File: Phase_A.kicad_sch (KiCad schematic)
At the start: 12 parts

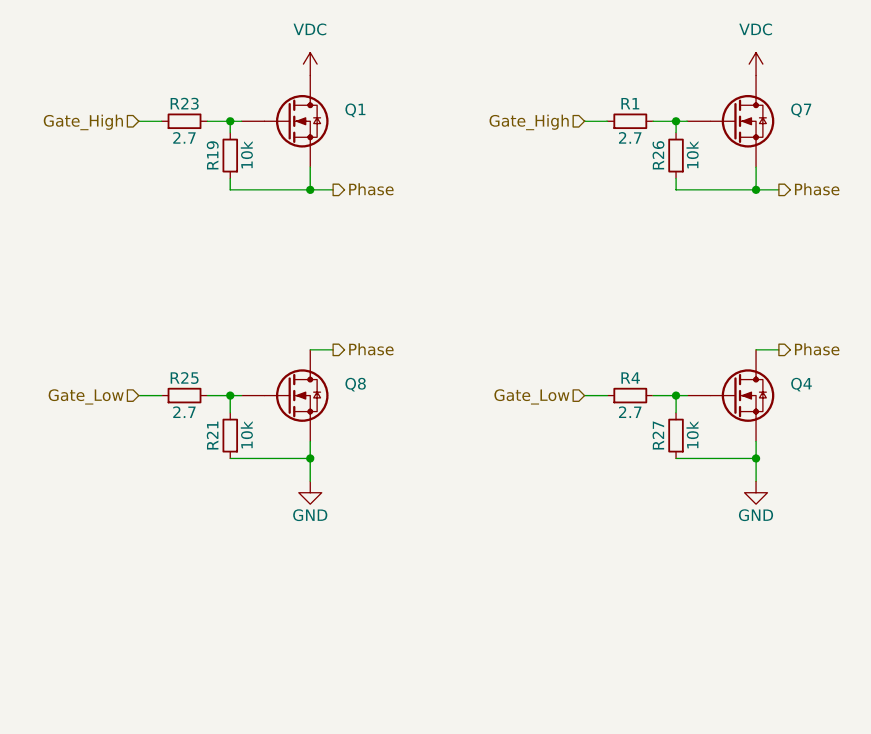
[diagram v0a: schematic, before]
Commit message: §3, §5, §6 схема: NetTie SW, ветвь выключения на позицию, C_gs, снабберы, RC на HI/LI
Driver.kicad_sch: SW драйвера — своя цепь через NetTie NT1–NT3; на HO и LO
R_on 0.82 Ом ∥ (D_off PMEG4010BEA + R_off 0 Ом), R106–R117, D30–D35; на HI/LI
R 0 Ом + C 100 пФ DNP (R118–R123, C118–C123).
Phase_A.kicad_sch: R_g 2.7 Ом 0805 -> 1 Ом 0603; C_gs 4.7 нФ DNP C100–C111;
снабберы LS и HS DNP (C112–C117, R100–R105).
ERC — 9 ошибок (база), netlist сверен по цепям: +57 компонентов, прочие связи
без изменений. ТЗ: Р3 — термистор остаётся на узле, Р10 — VDC→J6 можно
перекладывать.

Co-Authored-By: Claude Opus 5.5 <noreply@anthropic.com>
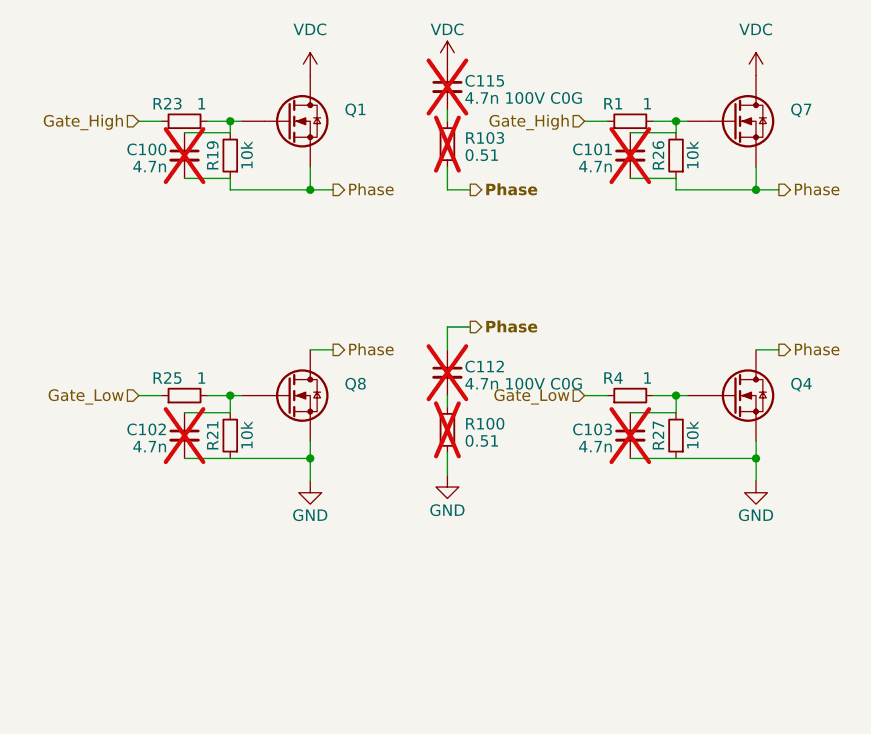
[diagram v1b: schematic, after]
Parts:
- added C100, C101, C102, C103: 4.7n, Capacitor_SMD:C_0603_1608Metric_Pad1.08x0.95mm_HandSolder, symbol Device:C_Small
- added C112, C115: 4.7n 100V C0G, Capacitor_SMD:C_0805_2012Metric_Pad1.18x1.45mm_HandSolder, symbol Device:C_Small
- added R100, R103: 0.51, Resistor_SMD:R_1206_3216Metric_Pad1.30x1.75mm_HandSolder, symbol Device:R_Small
- R1, R23, R25, R4: value 2.7 -> 1; footprint Resistor_SMD:R_0805_2012Metric_Pad1.20x1.40mm_HandSolder -> Resistor_SMD:R_0603_1608Metric_Pad0.98x0.95mm_HandSolder
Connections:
- net GND: now also C102.2, C103.2, R100.2
- net Phase: now also C100.2, C101.2, C112.1, R103.2
- net VDC: now also C115.1
- net at Q8.G, R21.2, R25.2: now also C102.1
- net at Q7.G, R1.2, R26.2: now also C101.1
- net at Q1.G, R19.2, R23.2: now also C100.1
- net at Q4.G, R27.2, R4.2: now also C103.1
- new net: C115.2, R103.1
- new net: C112.2, R100.1

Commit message: Схема, второй заход: ветвь выключения без R_off, керамика §4 (Р14, Р15)
R_off (R109–R111, R115–R117) убраны — D_off прямо от X к выводу драйвера;
R_on — 0603, D_off — стандартный SOD-323. Керамика петли C124–C135,
1 мкФ 100 В 1206, по 4 на фазу. ERC — 9 ошибок (база), netlist сверен.

Co-Authored-By: Claude Opus 5.5 <noreply@anthropic.com>
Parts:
- added C124, C125, C126, C127: 1u 100V X7R, Capacitor_SMD:C_1206_3216Metric_Pad1.33x1.80mm_HandSolder, symbol Device:C_Small
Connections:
- net GND: now also C124.2, C125.2, C126.2, C127.2
- net VDC: now also C124.1, C125.1, C126.1, C127.1

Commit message: WIP разводка: керамика §4 — по одному 1206 на фазу; лишние три на фазу убраны из схемы
1206 1u 100V (C124/C128/C132) в среднем ряду колонки стока HS, одинаково на
трёх фазах, у каждого своя пара виа (VDC и GND). Верхняя полоса над стоком
занята корпусами банок ЗПТ Ø10 (по футпринту до y 74.1), нижний ряд — R_g
нижнего HS; поэтому C125–C127, C129–C131, C133–C135 удалены из схемы и платы
(Р6, «по месту»). C110 переставлен вглубь полосы A (4 виа сдвинуты в полосе).
DRC: 0 ошибок, расхождений со схемой нет; ERC: 9 (база).

Co-Authored-By: Claude Opus 5.5 <noreply@anthropic.com>
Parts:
- removed C125, C126, C127: 1u 100V X7R, Capacitor_SMD:C_1206_3216Metric_Pad1.33x1.80mm_HandSolder, symbol Device:C_Small

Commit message: Д1, Д2: C_gs C100–C111 — 10 нФ C0G, ставятся; D_off D30–D35 — DNP (схема и плата); Д3 снят решением владельца
Co-Authored-By: Claude Opus 5.5 <noreply@anthropic.com>
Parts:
- C100, C101, C102, C103: value 4.7n -> 10n 50V C0G; Description P/N Capacitor SMD 50V -> Capacitor SMD 50V C0G; now fitted
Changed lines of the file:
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@@
 		(on_board yes)
 		(in_pos_files yes)
-		(dnp yes)
+		(dnp no)
 		(property "Reference" "C100"
 			(at 104.775 81.915 0)
@@
 			)
 		)
-		(property "Value" "4.7n"
+		(property "Value" "10n 50V C0G"
 			(at 104.775 83.82 0)
 			(show_name no)
@@
 			)
 		)
-		(property "Description P/N" "Capacitor SMD 50V"
+		(property "Description P/N" "Capacitor SMD 50V C0G"
 			(at 106.68 82.55 0)
 			(hide yes)
@@
 		(on_board yes)
 		(in_pos_files yes)
-		(dnp yes)
+		(dnp no)
 		(property "Reference" "C101"
 			(at 154.305 81.915 0)
@@
 			)
 		)
-		(property "Value" "4.7n"
+		(property "Value" "10n 50V C0G"
 			(at 154.305 83.82 0)
 			(show_name no)
@@
 			)
 		)
-		(property "Description P/N" "Capacitor SMD 50V"
+		(property "Description P/N" "Capacitor SMD 50V C0G"
 			(at 156.21 82.55 0)
 			(hide yes)
@@
 		(on_board yes)
 		(in_pos_files yes)
-		(dnp yes)
+		(dnp no)
 		(property "Reference" "C102"
 			(at 104.775 113.03 0)
@@
 			)
 		)
-		(property "Value" "4.7n"
+		(property "Value" "10n 50V C0G"
 			(at 104.775 114.935 0)
 			(show_name no)
@@
 			)
 		)
-		(property "Description P/N" "Capacitor SMD 50V"
+		(property "Description P/N" "Capacitor SMD 50V C0G"
 			(at 106.68 113.665 0)
 			(hide yes)
@@
 		(on_board yes)
 		(in_pos_files yes)
-		(dnp yes)
+		(dnp no)
 		(property "Reference" "C103"
 			(at 154.305 113.03 0)
@@
 			)
 		)
-		(property "Value" "4.7n"
+		(property "Value" "10n 50V C0G"
 			(at 154.305 114.935 0)
 			(show_name no)
@@
 			)
 		)
-		(property "Description P/N" "Capacitor SMD 50V"
+		(property "Description P/N" "Capacitor SMD 50V C0G"
 			(at 156.21 113.665 0)
 			(hide yes)

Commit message: Плата длиннее на 4 мм: банки ЗПТ, J4/J5, H1/H2 выше; снабберы §5 у выводов (C 0805 + R 0612 0.47 Ом, средняя точка — перемычка), 1206 C125/C129/C133 у стока HS, 0603 по две на фазу; DRC 0/0/0
Co-Authored-By: Claude Opus 5.5 <noreply@anthropic.com>
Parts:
- added C125: 1u 100V X7R, Capacitor_SMD:C_1206_3216Metric_Pad1.33x1.80mm_HandSolder, symbol Device:C_Small
- R100, R103: value 0.51 -> 0.47; footprint Resistor_SMD:R_1206_3216Metric_Pad1.30x1.75mm_HandSolder -> Resistor_SMD:R_0612_1632Metric_Pad1.18x3.40mm_HandSolder; Description P/N Resistor SMD 0.5W -> Resistor SMD 0612 1.5W
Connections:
- net GND: now also C125.2
- net VDC: now also C125.1
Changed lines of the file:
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@@
+	(symbol
+		(lib_id "Device:C_Small")
+		(at 120.65 137.16 0)
+		(unit 1)
+		(body_style 1)
+		(exclude_from_sim no)
+		(in_bom yes)
+		(on_board yes)
+		(in_pos_files yes)
+		(dnp no)
+		(property "Reference" "C125"
+			(at 121.92 136.525 0)
+			(show_name no)
+			(do_not_autoplace no)
+			(effects
+				(font
+					(size 1.27 1.27)
+				)
+				(justify left)
+			)
+		)
+		(property "Value" "1u 100V X7R"
+			(at 121.92 138.43 0)
+			(show_name no)
+			(do_not_autoplace no)
+			(effects
+				(font
+					(size 1.27 1.27)
+				)
+				(justify left)
+			)
+		)
+		(property "Footprint" "Capacitor_SMD:C_1206_3216Metric_Pad1.33x1.80mm_HandSolder"
+			(at 120.65 137.16 0)
+			(hide yes)
+			(show_name no)
+			(do_not_autoplace no)
+			(effects
+				(font
+					(size 1.27 1.27)
+				)
+			)
+		)
+		(property "Datasheet" ""
+			(at 120.65 137.16 0)
+			(hide yes)
+			(show_name no)
+			(do_not_autoplace no)
+			(effects
+				(font
+					(size 1.27 1.27)
+				)
+			)
+		)
+		(property "Description" ""
+			(at 120.65 137.16 0)
+			(hide yes)
+			(show_name no)
+			(do_not_autoplace no)
+			(effects
+				(font
+					(size 1.27 1.27)
+				)
+			)
+		)
+		(property "Description P/N" "Capacitor SMD 100V X7R"
+			(at 120.65 137.16 0)
+			(hide yes)
+			(show_name no)
+			(do_not_autoplace no)
+			(effects
+				(font
+					(size 1.27 1.27)
+				)
+			)
+		)
+		(pin "1"
+		)
+		(pin "2"
+		)
+		(instances
+			(project "Power"
+				(path "/7ff38f8b-11c9-43a1-8b76-b5e8c8de18e0/f977a2eb-d10b-44d6-a07c-b8311dd9b73f"
+					(reference "C125")
+					(unit 1)
+				)
+				(path "/7ff38f8b-11c9-43a1-8b76-b5e8c8de18e0/7176583c-694b-43e7-a08f-7dfec6a5a7f3"
+					(reference "C129")
+					(unit 1)
+				)
+				(path "/7ff38f8b-11c9-43a1-8b76-b5e8c8de18e0/fe135066-9555-4a85-b389-3791e4e86e93"
+					(reference "C133")
+					(unit 1)
+				)
+			)
+		)
+	)
+	(wire
+		(pts
+			(xy 105.41 134.62) (xy 120.65 134.62)
+		)
+		(stroke
+			(width 0)
+			(type default)
+		)
+	)
+	(wire
+		(pts
+			(xy 105.41 139.7) (xy 120.65 139.7)
+		)
+		(stroke
+			(width 0)
+			(type default)
+		)
+	)
 	(symbol
 		(lib_id "Device:C_Small")
@@
 			)
 		)
-		(property "Value" "0.51"
+		(property "Value" "0.47"
 			(at 137.795 82.55 0)
 			(show_name no)
@@
 			)
 		)
-		(property "Footprint" "Resistor_SMD:R_1206_3216Metric_Pad1.30x1.75mm_HandSolder"
+		(property "Footprint" "Resistor_SMD:R_0612_1632Metric_Pad1.18x3.40mm_HandSolder"
 			(at 135.89 81.28 0)
 			(hide yes)
@@
 			)
 		)
-		(property "Description P/N" "Resistor SMD 0.5W"
+		(property "Description P/N" "Resistor SMD 0612 1.5W"
 			(at 135.89 81.28 0)
 			(hide yes)
@@
 			)
 		)
-		(property "Value" "0.51"
+		(property "Value" "0.47"
 			(at 137.795 114.3 0)
 			(show_name no)
@@
 			)
 		)
-		(property "Footprint" "Resistor_SMD:R_1206_3216Metric_Pad1.30x1.75mm_HandSolder"
+		(property "Footprint" "Resistor_SMD:R_0612_1632Metric_Pad1.18x3.40mm_HandSolder"
 			(at 135.89 113.03 0)
 			(hide yes)
@@
 			)
 		)
-		(property "Description P/N" "Resistor SMD 0.5W"
+		(property "Description P/N" "Resistor SMD 0612 1.5W"
 			(at 135.89 113.03 0)
 			(hide yes)

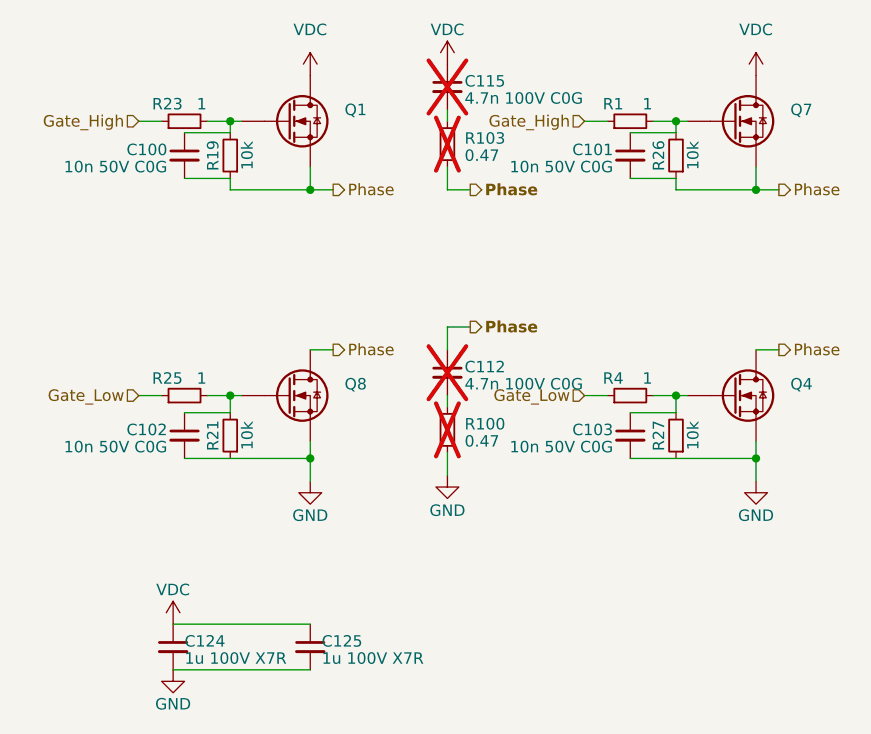
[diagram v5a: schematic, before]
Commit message: Решения владельца: предохранитель снят с платы (на соединительную плату, плата и корневой лист — как в d30010b); снаббер R — 2 × 0805 1 Ом параллельно (R100–R105 + R124–R129) в пределах прежних пэдов 0612; места под Y между J4/J5 — H5 CHASSIS винтом в радиатор, C135/C136 DNP, зазор 2 мм; снабберы на части первых плат rev0.1; цель ЭМС — CISPR 25 класс 3; DRC 0/0/0
Co-Authored-By: Claude Opus 5.5 <noreply@anthropic.com>
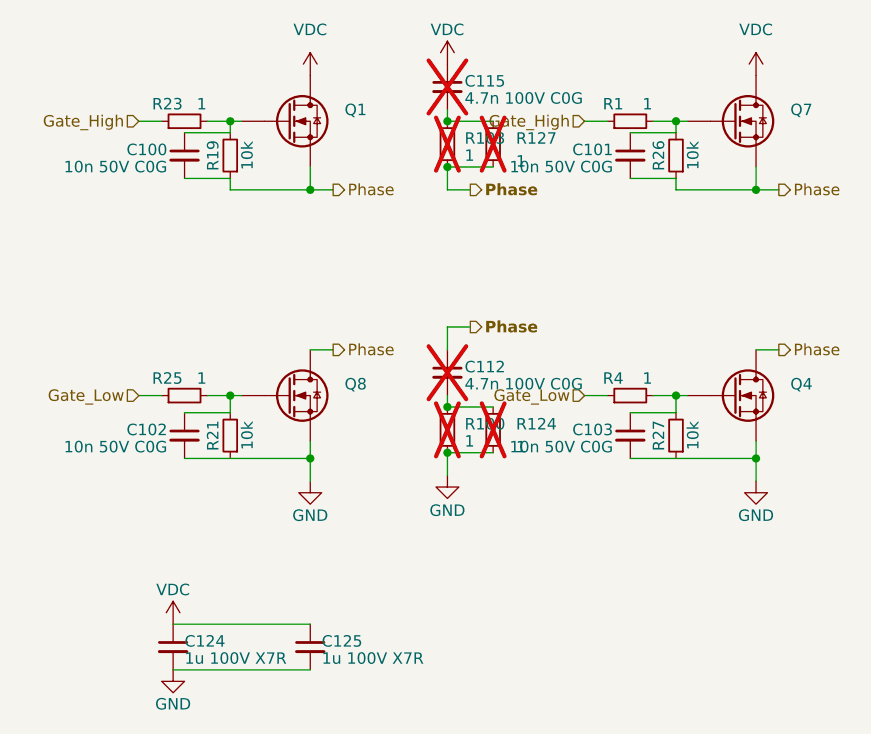
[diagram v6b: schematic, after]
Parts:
- added R124, R127: 1, Resistor_SMD:R_0805_2012Metric, symbol Device:R_Small
- R100, R103: value 0.47 -> 1; footprint Resistor_SMD:R_0612_1632Metric_Pad1.18x3.40mm_HandSolder -> Resistor_SMD:R_0805_2012Metric; Description P/N Resistor SMD 0612 1.5W -> Resistor SMD 0805 anti-surge 0.5W (ERJ-P06J1R0V)
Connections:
- net GND: now also R124.2
- net Phase: now also R127.2
- net at C115.2, R103.1: now also R127.1
- net at C112.2, R100.1: now also R124.1

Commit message: rev0.1-shift3: длина платы как у rev0.1-gnd (108.76 мм), блок и зона МК на 3 мм ниже, полоса 3 мм под снабберы
- shift3.sh с 515455d: верх (банки, J4/J5, H1/H2) на 3 мм выше; плечи у винтов прижимной пластины остаются с блоком; низ снят на 3 мм (lay_S3c.py)
- снабберы: R 1206 0.47 Ом anti-surge (HandSolder), C 0805 стандартные пэды; все шесть 0603 2.2 мкФ в полосе; 1206 C125/C129/C133 не поместились
- U7 на B.Cu под U5 (270°, линии CS/SCK/MISO/MOSI лесенкой, по одной виа); обвязка входов U6 на 2.05 мм выше; виа SWCLK_IN перенесена
- сшивка VDC/GND: 26 виа, 15 подобраны заново (cflow); VDC C/B/A 0.365/0.331/0.547, GND 0.316/0.171/0.194 мОм; узлы как на plus4
- geom.py: дуги и кривые Безье контура точно; strip_plan.py: нижняя граница перебора, совместный подбор 0603 и снабберов
- DRC 0/0/0, ERC 9/51, hv.py 24, track_scan 0; plus4.sh по-прежнему даёт плату ee0755d

Co-Authored-By: Claude Opus 5.5 <noreply@anthropic.com>
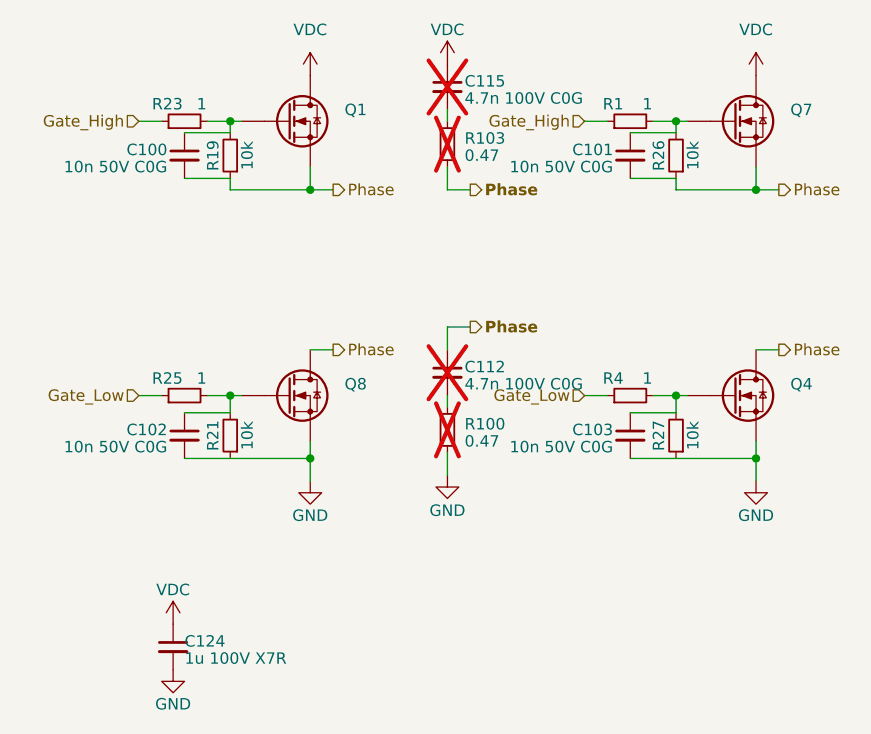
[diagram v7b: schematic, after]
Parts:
- removed C125: 1u 100V X7R, Capacitor_SMD:C_1206_3216Metric_Pad1.33x1.80mm_HandSolder, symbol Device:C_Small
- removed R124, R127: 1, Resistor_SMD:R_0805_2012Metric, symbol Device:R_Small
- C112, C115: footprint Capacitor_SMD:C_0805_2012Metric_Pad1.18x1.45mm_HandSolder -> Capacitor_SMD:C_0805_2012Metric
- R100, R103: value 1 -> 0.47; footprint Resistor_SMD:R_0805_2012Metric -> Resistor_SMD:R_1206_3216Metric_Pad1.30x1.75mm_HandSolder; Description P/N Resistor SMD 0805 anti-surge 0.5W (ERJ-P06J1R0V) -> Resistor SMD 1206 anti-surge 0.5W
